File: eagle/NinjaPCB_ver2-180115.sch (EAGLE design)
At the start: 76 parts, among them IC2 VNH5019/VNH3SP30-BNC, IC3 ANALOGSW_AD_SOT23-6NC, IC4 ANALOGSW_TI-SC70-5/6NC, IC5 MCP3551SNNC, IC6 NAU7802NC, J2 ATX24, J3 HEATER, J4 HEATER_TEMP, J5 PELTIER, Q2 IRF520NPBF, Q3 IRF520NPBF, U1 CJT1117-3.3-SOT223

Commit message: add memos
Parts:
- added R4: 10K 1/10W, Seeed-Resistor:SMD-RES-10K-5%-1/10W(0603)
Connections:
- net 3V3: now also R4.1
- net PEL_INB: now also R4.2
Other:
- note added: "Diff from ver2-170831: 1. IO0 is pulled up"
- note added: "NOTES: 1. (Rl, Rh) = IDEAL(30k, 15k), SOLDERED(20k, 10k)"
- note added: "Need to update : 1. Change Rx/Tx 2. MOSFET turns on above 4V, not 3V3 3. MOSFET is in wrong config IO0の接続がなんだかあやしい * 電源を入れた状態だと、IO0ボタンを押しても離してもTX(@ESP 端から3番目のピン)と導通している * 本来PUされているはずなのだがボタンを離した状態で2.47Vという中途半端な電圧"
- note removed: "NOTES: 1. MOSFET TURNS ON ABOVE 4V, not 3V3 2. (Rl, Rh) = IDEAL(30k, 15k), TEST(20k, 10k) 3. Change Rx/Tx 4. Pullup IO0 -done at next IO0の接続がなんだかあやしい * 電源を入れた状態だと、IO0ボタンを押しても離してもTX(@ESP 端から3番目のピン)と導通している * 本来PUされているはずなのだがボタンを離した状態で2.47Vという中途半端な電圧"
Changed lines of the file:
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@@
 <part name="U$1" library="adafruit" deviceset="2.1MMJACK" device="THM"/>
 <part name="RH2" library="PCR-RCL" deviceset="R0603" device="NC" value="30K HP"/>
+<part name="R4" library="Seeed-Resistor" deviceset="SMD-RES-10K-5%-1/10W(0603)" device="" value="10K 1/10W"/>
 </parts>
 <sheets>
@@
 <text x="34.29" y="233.68" size="3.81" layer="97">MCU</text>
 <text x="38.1" y="77.47" size="3.81" layer="97">POWER</text>
-<text x="171.45" y="26.67" size="1.778" layer="97">NOTES:
-1. MOSFET TURNS ON ABOVE 4V, not 3V3
-2. (Rl, Rh) = IDEAL(30k, 15k), TEST(20k, 10k)
-3. Change Rx/Tx
-4. Pullup IO0 -done at next
+<text x="165.1" y="12.7" size="1.778" layer="97">NOTES:
+1. (Rl, Rh) = IDEAL(30k, 15k), SOLDERED(20k, 10k)</text>
+<text x="165.1" y="31.75" size="1.778" layer="97">Need to update :
+1. Change Rx/Tx
+2. MOSFET turns on above 4V, not 3V3
+3. MOSFET is in wrong config
 IO0の接続がなんだかあやしい
 * 電源を入れた状態だと、IO0ボタンを押しても離してもTX(@ESP 端から3番目のピン)と導通している
 * 本来PUされているはずなのだがボタンを離した状態で2.47Vという中途半端な電圧</text>
+<text x="165.1" y="22.86" size="1.778" layer="97">Diff from ver2-170831:
+1. IO0 is pulled up</text>
 </plain>
 <instances>
@@
 <instance part="U$1" gate="G$1" x="97.79" y="53.34"/>
 <instance part="RH2" gate="G$1" x="228.6" y="205.74" rot="R90"/>
+<instance part="R4" gate="G$1" x="33.02" y="100.33"/>
 </instances>
 <busses>
@@
 <segment>
 <pinref part="3V6" gate="VCC" pin="VCC"/>
+<wire x1="24.13" y1="124.46" x2="26.67" y2="124.46" width="0.1524" layer="91"/>
 <pinref part="R9" gate="G$1" pin="1"/>
-<wire x1="24.13" y1="124.46" x2="29.21" y2="124.46" width="0.1524" layer="91"/>
+<pinref part="R4" gate="G$1" pin="1"/>
+<wire x1="26.67" y1="124.46" x2="29.21" y2="124.46" width="0.1524" layer="91"/>
+<wire x1="29.21" y1="100.33" x2="26.67" y2="100.33" width="0.1524" layer="91"/>
+<wire x1="26.67" y1="100.33" x2="26.67" y2="124.46" width="0.1524" layer="91"/>
+<junction x="26.67" y="124.46"/>
 </segment>
 </net>
@@
 <junction x="62.23" y="100.33"/>
 <label x="64.77" y="100.33" size="1.778" layer="95"/>
-</segment>
-</net>
+<pinref part="R4" gate="G$1" pin="2"/>
+<wire x1="39.37" y1="100.33" x2="36.83" y2="100.33" width="0.1524" layer="91"/>
+<junction x="39.37" y="100.33"/>
+</segment>
+</net>

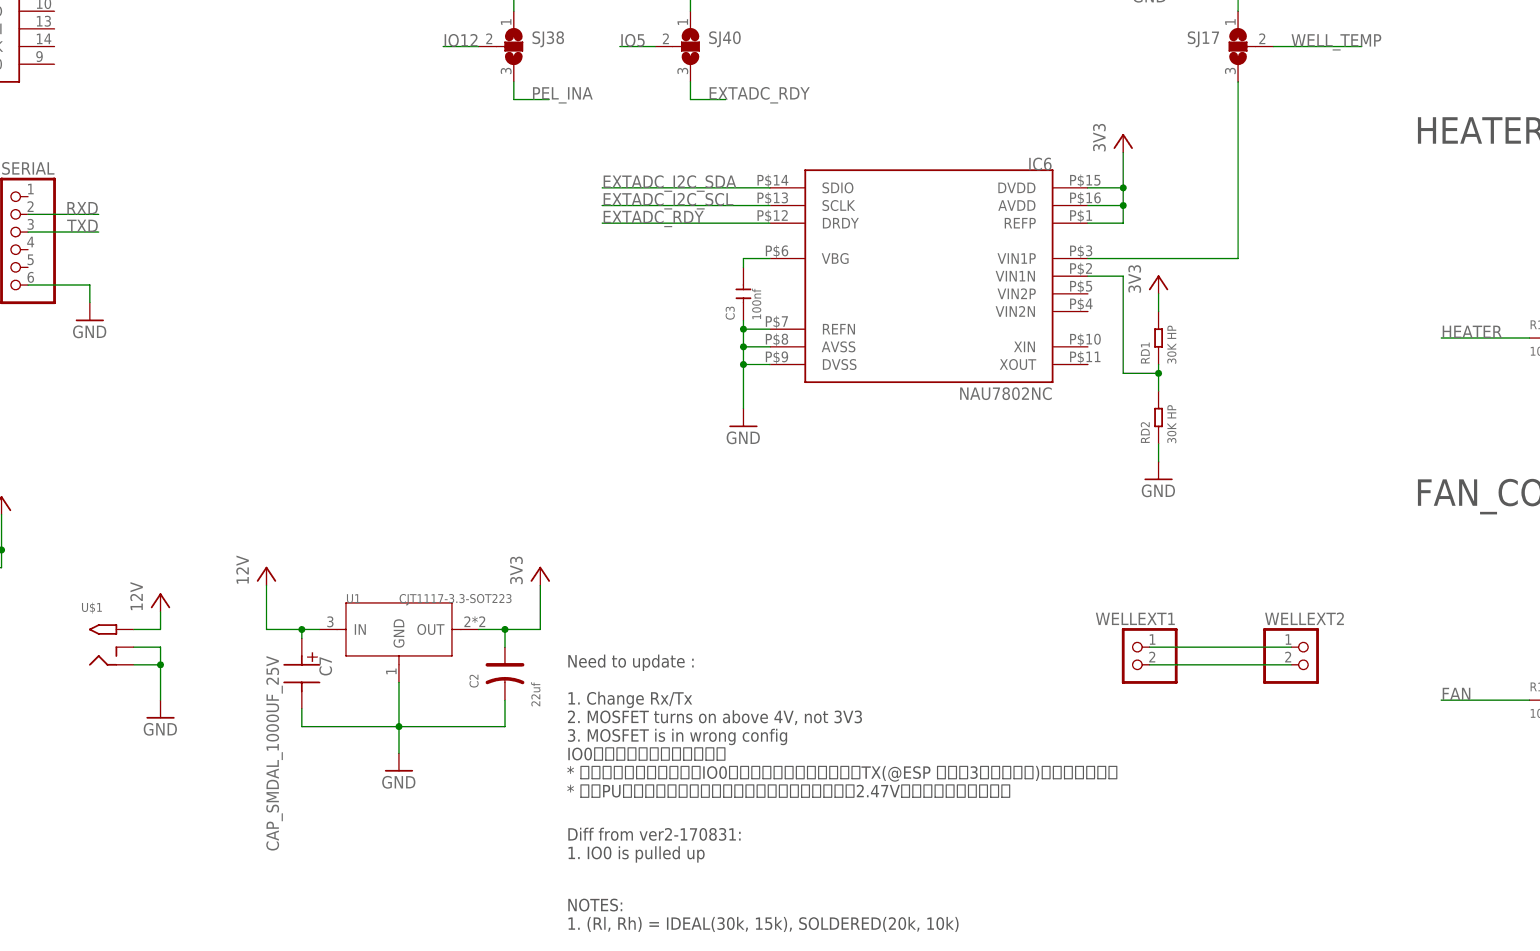
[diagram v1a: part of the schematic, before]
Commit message: pulldown HEATER to write
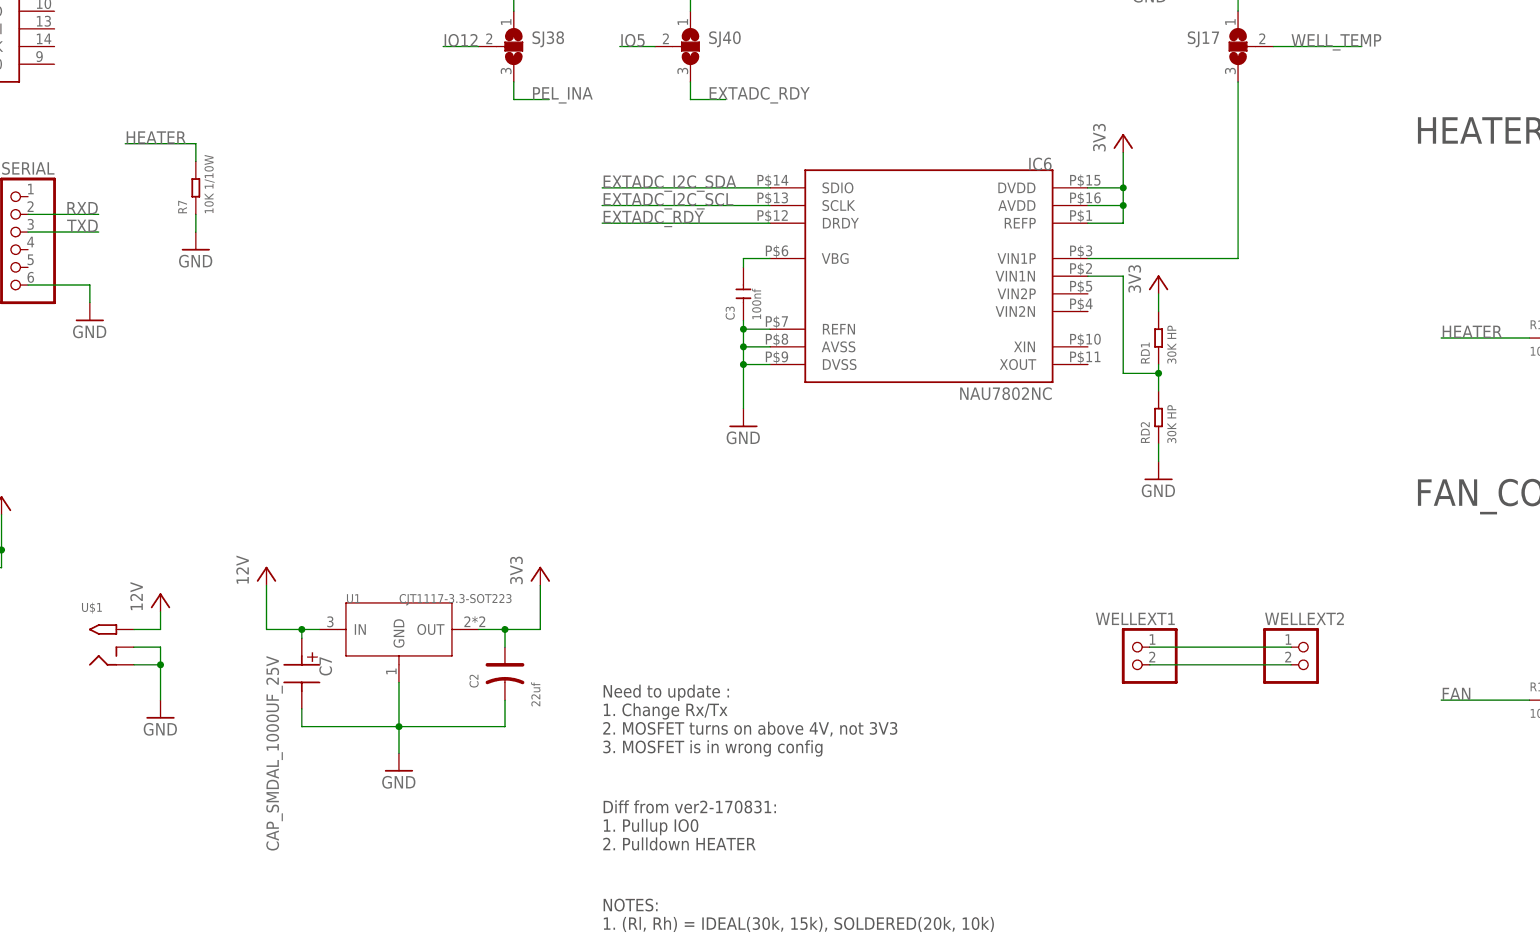
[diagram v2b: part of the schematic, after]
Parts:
- added R7: 10K 1/10W, Seeed-Resistor:SMD-RES-10K-5%-1/10W(0603)
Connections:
- net GND: now also R7.1
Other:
- note added: "Diff from ver2-170831: 1. Pullup IO0 2. Pulldown HEATER"
- note added: "Need to update : 1. Change Rx/Tx 2. MOSFET turns on above 4V, not 3V3 3. MOSFET is in wrong config"
- note removed: "Diff from ver2-170831: 1. IO0 is pulled up"
- note removed: "Need to update : 1. Change Rx/Tx 2. MOSFET turns on above 4V, not 3V3 3. MOSFET is in wrong config IO0の接続がなんだかあやしい * 電源を入れた状態だと、IO0ボタンを押しても離してもTX(@ESP 端から3番目のピン)と導通している * 本来PUされているはずなのだがボタンを離した状態で2.47Vという中途半端な電圧"
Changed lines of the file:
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@@
 <setting verticaltext="up"/>
 </settings>
-<grid distance="0.1" unitdist="inch" unit="inch" style="lines" multiple="1" display="no" altdistance="0.01" altunitdist="inch" altunit="inch"/>
+<grid distance="0.05" unitdist="inch" unit="inch" style="lines" multiple="1" display="no" altdistance="0.01" altunitdist="inch" altunit="inch"/>
 <layers>
 <layer number="1" name="Top" color="4" fill="1" visible="no" active="no"/>
@@
 <part name="RH2" library="PCR-RCL" deviceset="R0603" device="NC" value="30K HP"/>
 <part name="R4" library="Seeed-Resistor" deviceset="SMD-RES-10K-5%-1/10W(0603)" device="" value="10K 1/10W"/>
+<part name="GND11" library="supply1" deviceset="GND" device=""/>
+<part name="R7" library="Seeed-Resistor" deviceset="SMD-RES-10K-5%-1/10W(0603)" device="" value="10K 1/10W"/>
 </parts>
 <sheets>
@@
 <text x="34.29" y="233.68" size="3.81" layer="97">MCU</text>
 <text x="38.1" y="77.47" size="3.81" layer="97">POWER</text>
-<text x="165.1" y="12.7" size="1.778" layer="97">NOTES:
+<text x="170.18" y="12.7" size="1.778" layer="97">NOTES:
 1. (Rl, Rh) = IDEAL(30k, 15k), SOLDERED(20k, 10k)</text>
-<text x="165.1" y="31.75" size="1.778" layer="97">Need to update :
+<text x="170.18" y="38.1" size="1.778" layer="97">Need to update :
 1. Change Rx/Tx
 2. MOSFET turns on above 4V, not 3V3
-3. MOSFET is in wrong config
-IO0の接続がなんだかあやしい
-* 電源を入れた状態だと、IO0ボタンを押しても離してもTX(@ESP 端から3番目のピン)と導通している
-* 本来PUされているはずなのだがボタンを離した状態で2.47Vという中途半端な電圧</text>
-<text x="165.1" y="22.86" size="1.778" layer="97">Diff from ver2-170831:
-1. IO0 is pulled up</text>
+3. MOSFET is in wrong config</text>
+<text x="170.18" y="24.13" size="1.778" layer="97">Diff from ver2-170831:
+1. Pullup IO0
+2. Pulldown HEATER</text>
 </plain>
 <instances>
@@
 <instance part="RH2" gate="G$1" x="228.6" y="205.74" rot="R90"/>
 <instance part="R4" gate="G$1" x="33.02" y="100.33"/>
+<instance part="GND11" gate="1" x="111.76" y="110.49"/>
+<instance part="R7" gate="G$1" x="111.76" y="119.38" rot="R90"/>
 </instances>
 <busses>
@@
 <wire x1="363.22" y1="223.52" x2="363.22" y2="218.44" width="0.1524" layer="91"/>
 </segment>
+<segment>
+<pinref part="R7" gate="G$1" pin="1"/>
+<pinref part="GND11" gate="1" pin="GND"/>
+<wire x1="111.76" y1="115.57" x2="111.76" y2="113.03" width="0.1524" layer="91"/>
+</segment>
 </net>
 <net name="3V3" class="0">
@@
 <label x="21.59" y="203.2" size="1.778" layer="95"/>
 </segment>
+<segment>
+<wire x1="111.76" y1="123.19" x2="111.76" y2="125.73" width="0.1524" layer="91"/>
+<wire x1="111.76" y1="125.73" x2="101.6" y2="125.73" width="0.1524" layer="91"/>
+<label x="101.6" y="125.73" size="1.778" layer="95"/>
+</segment>
 </net>

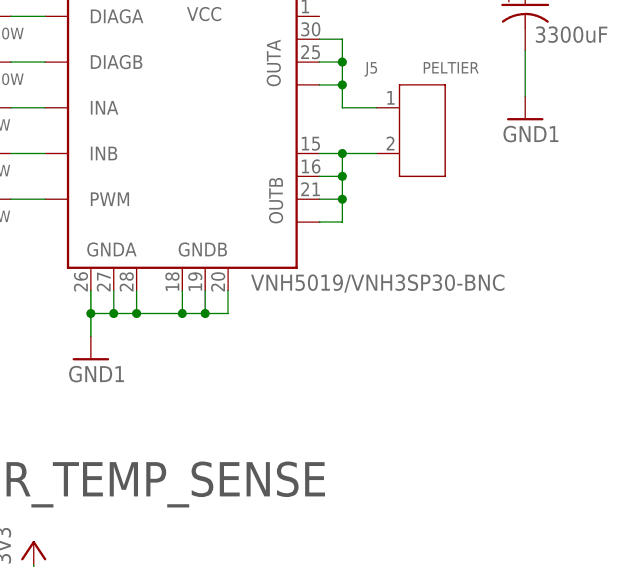
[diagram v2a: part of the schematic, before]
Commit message: VNH5019 doesnot have same pinout as VNH3SP30
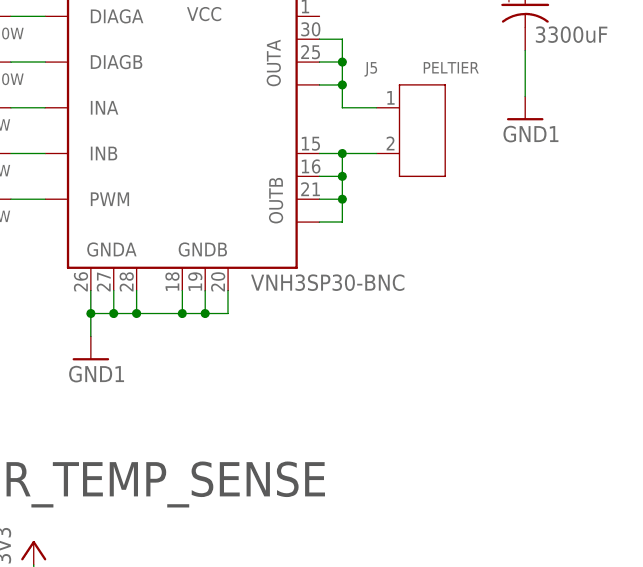
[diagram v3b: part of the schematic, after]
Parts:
- IC2: value VNH5019/VNH3SP30-BNC -> VNH3SP30-BNC; device st-microelectronics:VNH5019/VNH3SP30-BNC -> st-microelectronics:VNH3SP30-BNC
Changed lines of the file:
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@@
 <part name="GND21" library="openpcr" deviceset="GND1" device=""/>
 <part name="SJ17" library="jumper" deviceset="SJ2W" device=""/>
-<part name="IC2" library="st-microelectronics" deviceset="VNH5019/VNH3SP30-B" device="NC" value="VNH5019/VNH3SP30-BNC"/>
+<part name="IC2" library="st-microelectronics" deviceset="VNH3SP30-B" device="NC" value="VNH3SP30-BNC"/>
 <part name="U$1" library="adafruit" deviceset="2.1MMJACK" device="THM"/>
 <part name="RH2" library="PCR-RCL" deviceset="R0603" device="NC" value="30K HP"/>
